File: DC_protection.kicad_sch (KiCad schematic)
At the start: 15 parts

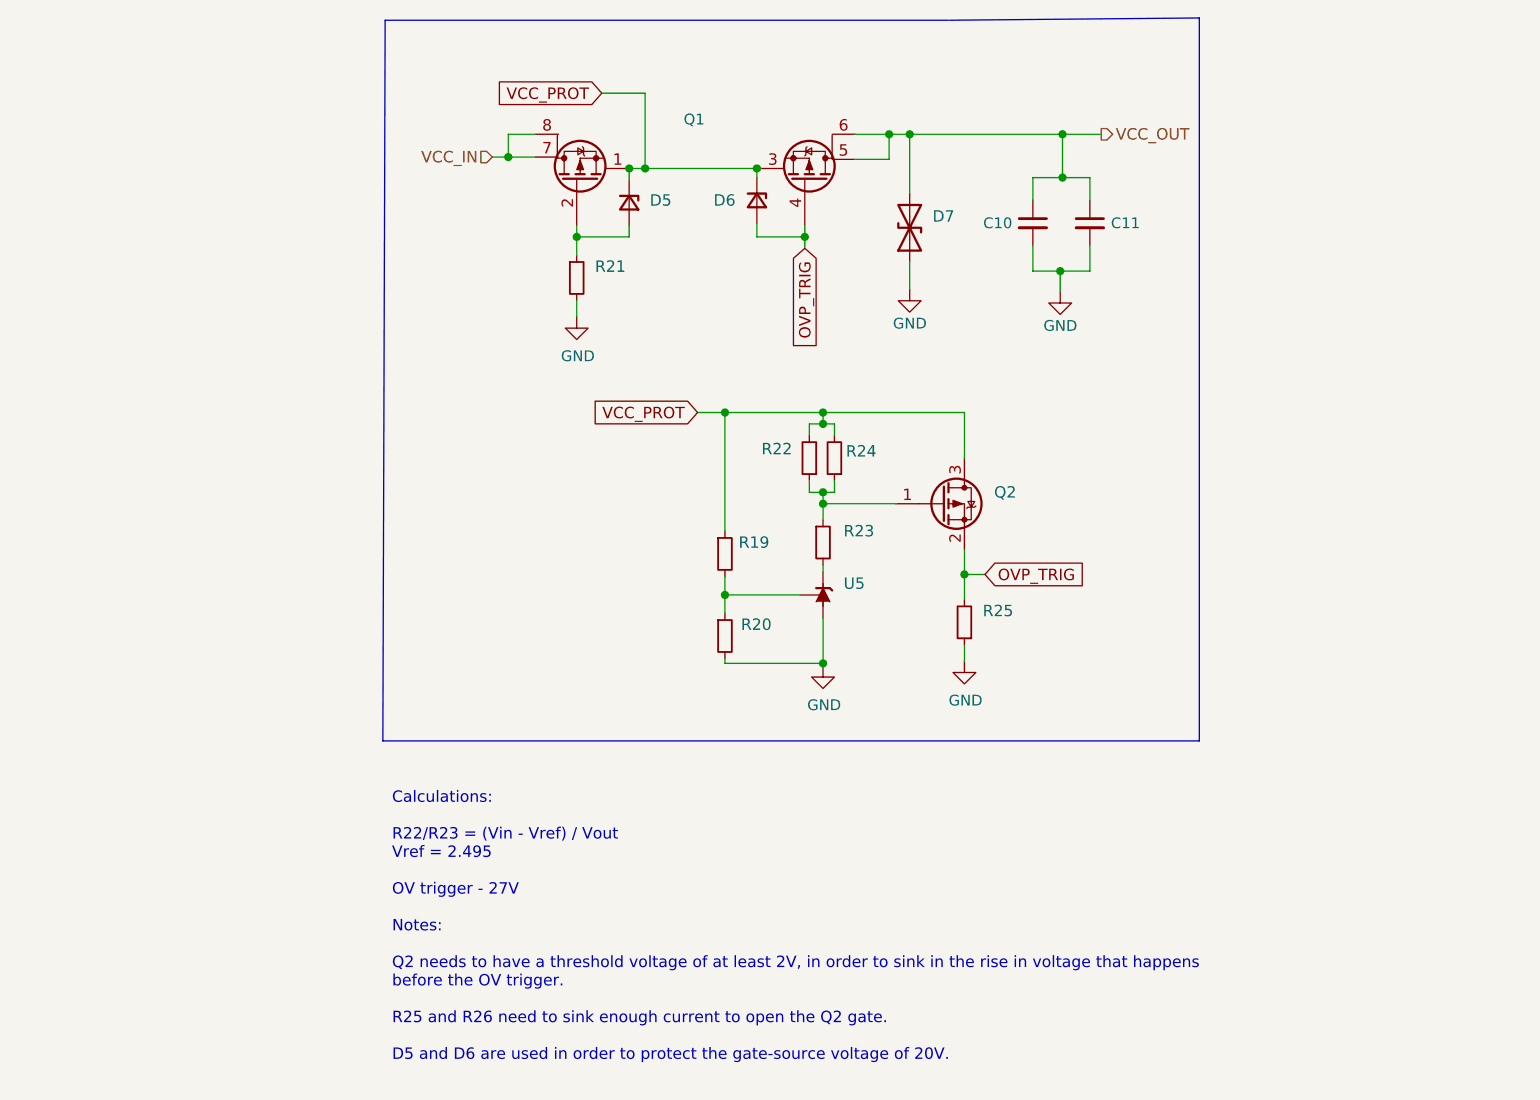
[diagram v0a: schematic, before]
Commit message: Redid symbol value and footprints for DC_Prot. Dont relink sub-schematics i guess..
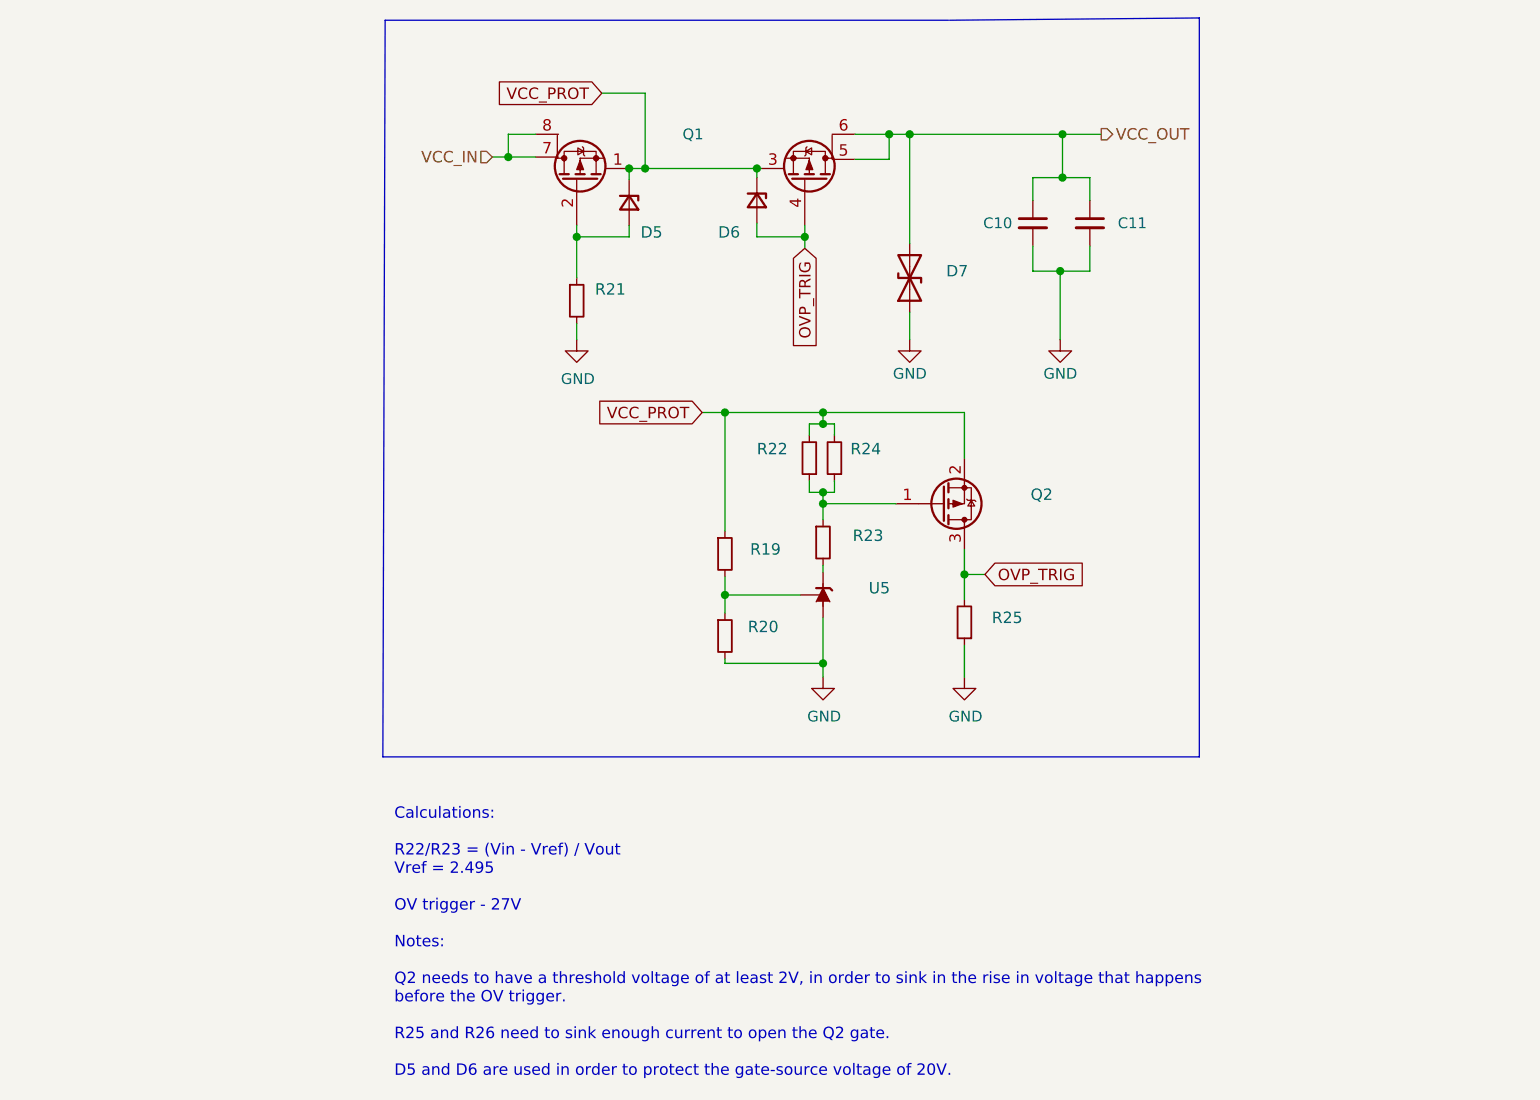
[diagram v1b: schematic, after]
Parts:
- C10, C11, D5, D6, D7, Q2, R19, R20, R21, R22, R23, R24, R25, U5: value ~ -> (none)
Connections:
- net OVP_TRIG: now also Q2.3 (D); no longer Q2.2 (S)
- net VCC_PROT: now also Q2.2 (S); no longer Q2.3 (D)
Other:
- moved on the sheet: D7, R21

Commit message: Exported updated gerbers
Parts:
- C10: value (none) -> 1uF; footprint (none) -> Capacitor_SMD:C_0805_2012Metric
- C11: value (none) -> 100nF; footprint (none) -> Capacitor_SMD:C_0603_1608Metric
- D5, D6: value (none) -> 16V TVS
- D7: value (none) -> 27V TVS; footprint (none) -> Diode_SMD:D_SOD-523
- Q1: value ~ -> VBA4658; footprint (none) -> Package_SO:SO-8_3.9x4.9mm_P1.27mm
- Q2: value (none) -> NCE60P04Y; footprint (none) -> Package_TO_SOT_SMD:SOT-23
- R19: value (none) -> 97.6KΩ; footprint (none) -> Resistor_SMD:R_0603_1608Metric
- R20: value (none) -> 10KΩ; footprint (none) -> Resistor_SMD:R_0603_1608Metric
- R21, R25: value (none) -> 100KΩ; footprint (none) -> Resistor_SMD:R_0603_1608Metric
- R22, R24: value (none) -> 2KΩ; footprint (none) -> Resistor_SMD:R_0603_1608Metric
- R23: value (none) -> 3.2KΩ; footprint (none) -> Resistor_SMD:R_0603_1608Metric
- U5: value (none) -> TL431DBZ
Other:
- note added: "OverVoltage Detection"
- note added: "Power"
- moved on the sheet: C10, C11, D5, D6, D7, Q1, Q2, R19, R20, R21, R22, R23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

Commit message: Cleanup of schematic, and final gerbers
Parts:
- D5, D6: footprint (none) -> Diode_SMD:D_SOD-323
- U5: footprint (none) -> Package_TO_SOT_SMD:SOT-23
- renumbered R21 to R19, R19 to R20, R20 to R21
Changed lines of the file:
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@@
       (effects (font (size 1.27 1.27)) (justify left))
     )
-    (property "Footprint" "" (id 2) (at 87.122 74.168 90)
-      (effects (font (size 1.27 1.27)) hide)
-    )
-    (property "Datasheet" "~" (id 3) (at 87.122 74.168 90)
+    (property "Footprint" "Diode_SMD:D_SOD-323" (id 2) (at 87.122 74.168 90)
+      (effects (font (size 1.27 1.27)) hide)
+    )
+    (property "Datasheet" "https://datasheet.lcsc.com/lcsc/1912111437_Shandong-Jingdao-Microelectronics-BZT52C16S_C353553.pdf" (id 3) (at 87.122 74.168 90)
       (effects (font (size 1.27 1.27)) hide)
     )
@@
   (symbol (lib_id "power:GND") (at 118.364 89.408 0) (unit 1)
     (in_bom yes) (on_board yes)
-    (property "Reference" "#PWR055" (id 0) (at 118.364 95.758 0)
+    (property "Reference" "#PWR054" (id 0) (at 118.364 95.758 0)
       (effects (font (size 1.2 1.2)) hide)
     )
@@
   (symbol (lib_id "Device:R_Small") (at 168.91 78.74 0) (unit 1)
     (in_bom yes) (on_board yes)
-    (property "Reference" "R19" (id 0) (at 171.704 78.232 0)
+    (property "Reference" "R20" (id 0) (at 171.704 78.232 0)
       (effects (font (size 1.27 1.27)) (justify left))
     )
@@
   (symbol (lib_id "Device:R_Small") (at 81.28 85.09 0) (unit 1)
     (in_bom yes) (on_board yes) (fields_autoplaced)
-    (property "Reference" "R21" (id 0) (at 83.312 83.8199 0)
+    (property "Reference" "R19" (id 0) (at 83.312 83.8199 0)
       (effects (font (size 1.27 1.27)) (justify left))
     )
@@
       (effects (font (size 1.27 1.27)) (justify right))
     )
-    (property "Footprint" "" (id 2) (at 183.642 83.312 0)
+    (property "Footprint" "Package_TO_SOT_SMD:SOT-23" (id 2) (at 183.642 83.312 0)
       (effects (font (size 1.27 1.27) italic) hide)
     )
@@
   (symbol (lib_id "power:GND") (at 81.28 89.408 0) (unit 1)
     (in_bom yes) (on_board yes)
-    (property "Reference" "#PWR052" (id 0) (at 81.28 95.758 0)
+    (property "Reference" "#PWR053" (id 0) (at 81.28 95.758 0)
       (effects (font (size 1.2 1.2)) hide)
     )
@@
       (effects (font (size 1.27 1.27)) (justify left))
     )
-    (property "Footprint" "" (id 2) (at 101.346 73.914 90)
-      (effects (font (size 1.27 1.27)) hide)
-    )
-    (property "Datasheet" "~" (id 3) (at 101.346 73.914 90)
+    (property "Footprint" "Diode_SMD:D_SOD-323" (id 2) (at 101.346 73.914 90)
+      (effects (font (size 1.27 1.27)) hide)
+    )
+    (property "Datasheet" "https://datasheet.lcsc.com/lcsc/1912111437_Shandong-Jingdao-Microelectronics-BZT52C16S_C353553.pdf" (id 3) (at 101.346 73.914 90)
       (effects (font (size 1.27 1.27)) hide)
     )
@@
   (symbol (lib_id "Device:R_Small") (at 168.91 87.884 0) (unit 1)
     (in_bom yes) (on_board yes)
-    (property "Reference" "R20" (id 0) (at 171.45 86.868 0)
+    (property "Reference" "R21" (id 0) (at 171.45 86.868 0)
       (effects (font (size 1.27 1.27)) (justify left))
     )
@@
   (symbol (lib_id "power:GND") (at 195.58 92.456 0) (unit 1)
     (in_bom yes) (on_board yes)
-    (property "Reference" "#PWR054" (id 0) (at 195.58 98.806 0)
+    (property "Reference" "#PWR057" (id 0) (at 195.58 98.806 0)
       (effects (font (size 1.2 1.2)) hide)
     )
@@
   (symbol (lib_id "power:GND") (at 179.832 92.456 0) (unit 1)
     (in_bom yes) (on_board yes)
-    (property "Reference" "#PWR053" (id 0) (at 179.832 98.806 0)
+    (property "Reference" "#PWR056" (id 0) (at 179.832 98.806 0)
       (effects (font (size 1.2 1.2)) hide)
     )
@@
   (symbol (lib_id "power:GND") (at 135.128 89.408 0) (unit 1)
     (in_bom yes) (on_board yes)
-    (property "Reference" "#PWR056" (id 0) (at 135.128 95.758 0)
-      (effects (font (size 1.2 1.2)) hide)
-    )
+    (property "Reference" "#PWR055" (id 0) (at 135.128 95.758 0)
+      (effects (font (size 1.2 1.2)) hide)
+    )

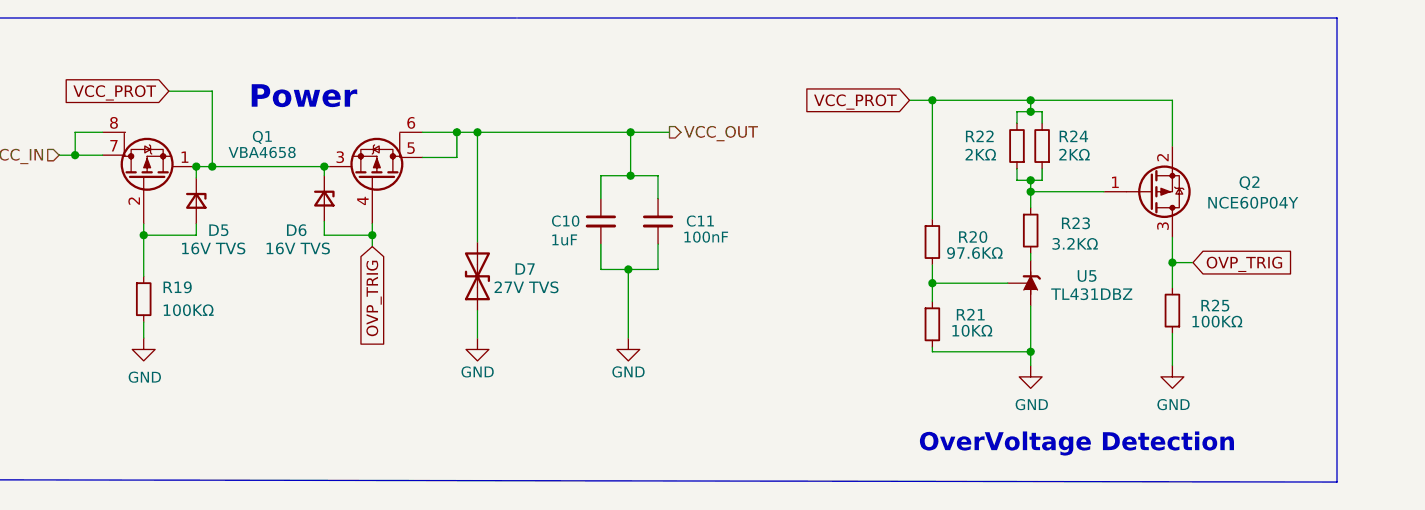
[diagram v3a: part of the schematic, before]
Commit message: Latest revision: 3v3 LDO replaced with buck converter, 5v0 buck replaced, LED configuration changed, speaker terminals replaced with sping connector, and new audio pepriheral FPC connector added. Besides this all data traces have been rerouted, the board has been shortened about 8mm.
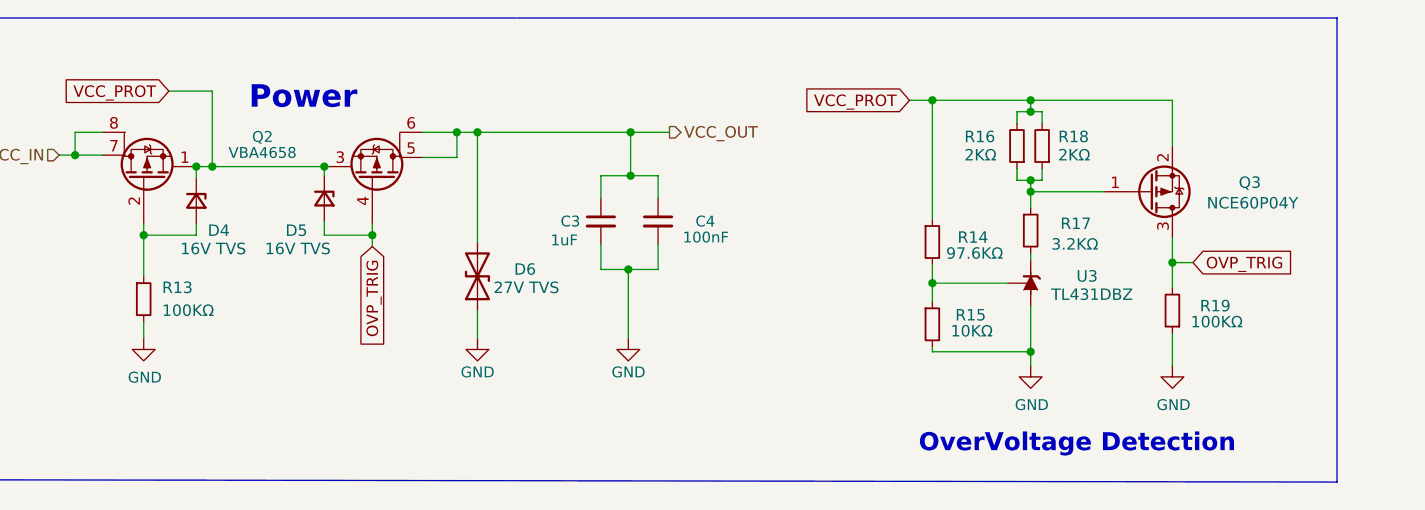
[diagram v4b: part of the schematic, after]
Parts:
- renumbered C10 to C3, C11 to C4, D5 to D4, D6 to D5, D7 to D6, Q1 to Q2, Q2 to Q3, R19 to R13, R20 to R14, R21 to R15, R22 to R16, R23 to R17, R24 to R18, R25 to R19, U5 to U3
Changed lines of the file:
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@@
   (symbol (lib_id "muVoxSyms:VBA4311") (at 81.28 70.358 0) (unit 1)
     (in_bom yes) (on_board yes)
-    (property "Reference" "Q1" (id 0) (at 94.488 67.056 0)
+    (property "Reference" "Q2" (id 0) (at 94.488 67.056 0)
       (effects (font (size 1.2 1.2)))
     )
@@
   (symbol (lib_id "Device:R_Small") (at 179.832 77.47 0) (unit 1)
     (in_bom yes) (on_board yes)
-    (property "Reference" "R23" (id 0) (at 183.134 76.708 0)
+    (property "Reference" "R17" (id 0) (at 183.134 76.708 0)
       (effects (font (size 1.27 1.27)) (justify left))
     )
@@
   (symbol (lib_id "Device:R_Small") (at 195.58 86.36 180) (unit 1)
     (in_bom yes) (on_board yes)
-    (property "Reference" "R25" (id 0) (at 198.628 85.852 0)
+    (property "Reference" "R19" (id 0) (at 198.628 85.852 0)
       (effects (font (size 1.27 1.27)) (justify right))
     )
@@
   (symbol (lib_id "Device:D_Zener_Small") (at 87.122 74.168 270) (unit 1)
     (in_bom yes) (on_board yes)
-    (property "Reference" "D5" (id 0) (at 88.392 77.47 90)
+    (property "Reference" "D4" (id 0) (at 88.392 77.47 90)
       (effects (font (size 1.27 1.27)) (justify left))
     )
@@
   (symbol (lib_id "power:GND") (at 118.364 89.408 0) (unit 1)
     (in_bom yes) (on_board yes)
-    (property "Reference" "#PWR054" (id 0) (at 118.364 95.758 0)
+    (property "Reference" "#PWR050" (id 0) (at 118.364 95.758 0)
       (effects (font (size 1.2 1.2)) hide)
     )
@@
   (symbol (lib_id "Device:R_Small") (at 168.91 78.74 0) (unit 1)
     (in_bom yes) (on_board yes)
-    (property "Reference" "R20" (id 0) (at 171.704 78.232 0)
+    (property "Reference" "R14" (id 0) (at 171.704 78.232 0)
       (effects (font (size 1.27 1.27)) (justify left))
     )
@@
   (symbol (lib_id "Device:C_Small") (at 132.08 76.454 0) (unit 1)
     (in_bom yes) (on_board yes)
-    (property "Reference" "C10" (id 0) (at 129.794 76.454 0)
+    (property "Reference" "C3" (id 0) (at 129.794 76.454 0)
       (effects (font (size 1.2 1.2)) (justify right))
     )
@@
   (symbol (lib_id "Device:C_Small") (at 138.43 76.454 0) (unit 1)
     (in_bom yes) (on_board yes)
-    (property "Reference" "C11" (id 0) (at 144.78 76.454 0)
+    (property "Reference" "C4" (id 0) (at 144.78 76.454 0)
       (effects (font (size 1.2 1.2)) (justify right))
     )
@@
   (symbol (lib_id "Device:R_Small") (at 181.102 68.072 180) (unit 1)
     (in_bom yes) (on_board yes)
-    (property "Reference" "R24" (id 0) (at 182.88 67.056 0)
+    (property "Reference" "R18" (id 0) (at 182.88 67.056 0)
       (effects (font (size 1.27 1.27)) (justify right))
     )
@@
   (symbol (lib_id "Device:Q_PMOS_GSD") (at 193.04 73.152 0) (mirror x) (unit 1)
     (in_bom yes) (on_board yes)
-    (property "Reference" "Q2" (id 0) (at 202.946 72.136 0)
+    (property "Reference" "Q3" (id 0) (at 202.946 72.136 0)
       (effects (font (size 1.27 1.27)) (justify left))
     )
@@
   (symbol (lib_id "Device:R_Small") (at 81.28 85.09 0) (unit 1)
     (in_bom yes) (on_board yes) (fields_autoplaced)
-    (property "Reference" "R19" (id 0) (at 83.312 83.8199 0)
+    (property "Reference" "R13" (id 0) (at 83.312 83.8199 0)
       (effects (font (size 1.27 1.27)) (justify left))
     )
@@
   (symbol (lib_id "Reference_Voltage:TL431DBZ") (at 179.832 83.312 90) (unit 1)
     (in_bom yes) (on_board yes)
-    (property "Reference" "U5" (id 0) (at 184.912 82.55 90)
+    (property "Reference" "U3" (id 0) (at 184.912 82.55 90)
       (effects (font (size 1.27 1.27)) (justify right))
     )
@@
   (symbol (lib_id "power:GND") (at 81.28 89.408 0) (unit 1)
     (in_bom yes) (on_board yes)
-    (property "Reference" "#PWR053" (id 0) (at 81.28 95.758 0)
+    (property "Reference" "#PWR049" (id 0) (at 81.28 95.758 0)
       (effects (font (size 1.2 1.2)) hide)
     )
@@
   (symbol (lib_id "Device:D_Zener_Small") (at 101.346 73.914 270) (unit 1)
     (in_bom yes) (on_board yes)
-    (property "Reference" "D6" (id 0) (at 97.028 77.47 90)
+    (property "Reference" "D5" (id 0) (at 97.028 77.47 90)
       (effects (font (size 1.27 1.27)) (justify left))
     )
@@
   (symbol (lib_id "Device:D_TVS") (at 118.364 82.55 90) (unit 1)
     (in_bom yes) (on_board yes)
-    (property "Reference" "D7" (id 0) (at 122.428 81.788 90)
+    (property "Reference" "D6" (id 0) (at 122.428 81.788 90)
       (effects (font (size 1.27 1.27)) (justify right))
     )
@@
   (symbol (lib_id "Device:R_Small") (at 168.91 87.884 0) (unit 1)
     (in_bom yes) (on_board yes)
-    (property "Reference" "R21" (id 0) (at 171.45 86.868 0)
+    (property "Reference" "R15" (id 0) (at 171.45 86.868 0)
       (effects (font (size 1.27 1.27)) (justify left))
     )
@@
   (symbol (lib_id "power:GND") (at 195.58 92.456 0) (unit 1)
     (in_bom yes) (on_board yes)
-    (property "Reference" "#PWR057" (id 0) (at 195.58 98.806 0)
+    (property "Reference" "#PWR053" (id 0) (at 195.58 98.806 0)
       (effects (font (size 1.2 1.2)) hide)
     )
@@
   (symbol (lib_id "Device:R_Small") (at 178.308 68.072 180) (unit 1)
     (in_bom yes) (on_board yes)
-    (property "Reference" "R22" (id 0) (at 172.466 67.056 0)
+    (property "Reference" "R16" (id 0) (at 172.466 67.056 0)
       (effects (font (size 1.27 1.27)) (justify right))
     )
@@
   (symbol (lib_id "power:GND") (at 179.832 92.456 0) (unit 1)
     (in_bom yes) (on_board yes)
-    (property "Reference" "#PWR056" (id 0) (at 179.832 98.806 0)
+    (property "Reference" "#PWR052" (id 0) (at 179.832 98.806 0)
       (effects (font (size 1.2 1.2)) hide)
     )
@@
   (symbol (lib_id "power:GND") (at 135.128 89.408 0) (unit 1)
     (in_bom yes) (on_board yes)
-    (property "Reference" "#PWR055" (id 0) (at 135.128 95.758 0)
-      (effects (font (size 1.2 1.2)) hide)
-    )
+    (property "Reference" "#PWR051" (id 0) (at 135.128 95.758 0)
+      (effects (font (size 1.2 1.2)) hide)
+    )
